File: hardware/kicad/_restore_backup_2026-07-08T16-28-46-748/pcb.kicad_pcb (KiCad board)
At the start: 2 copper layers, 56.1 x 59 mm, 7 parts, among them J1 ENCODER, J2 MOTOR, J3 12V MOTOR, U1 Dual_L298N_H_Bridge

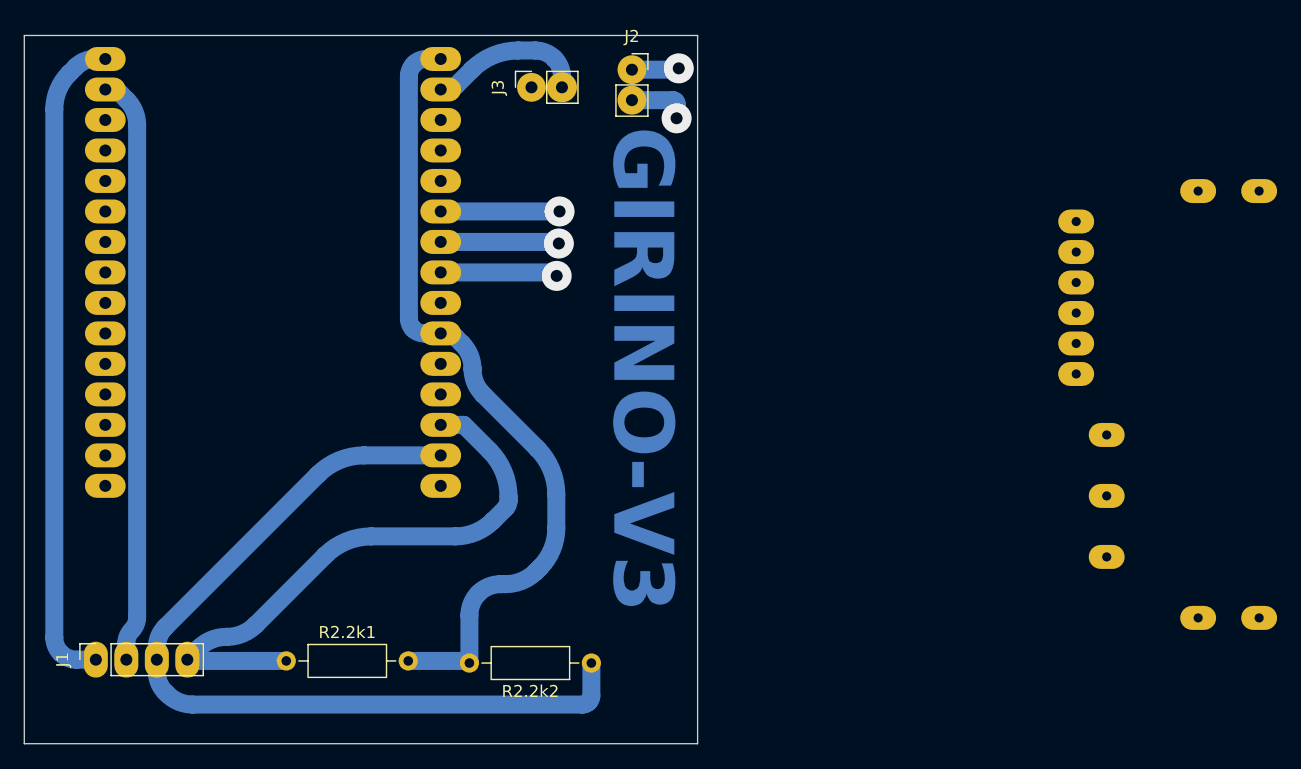
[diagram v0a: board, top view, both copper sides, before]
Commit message: fix:tirando o divisor de tensão e adcionando a forma correta de leitura do encoder
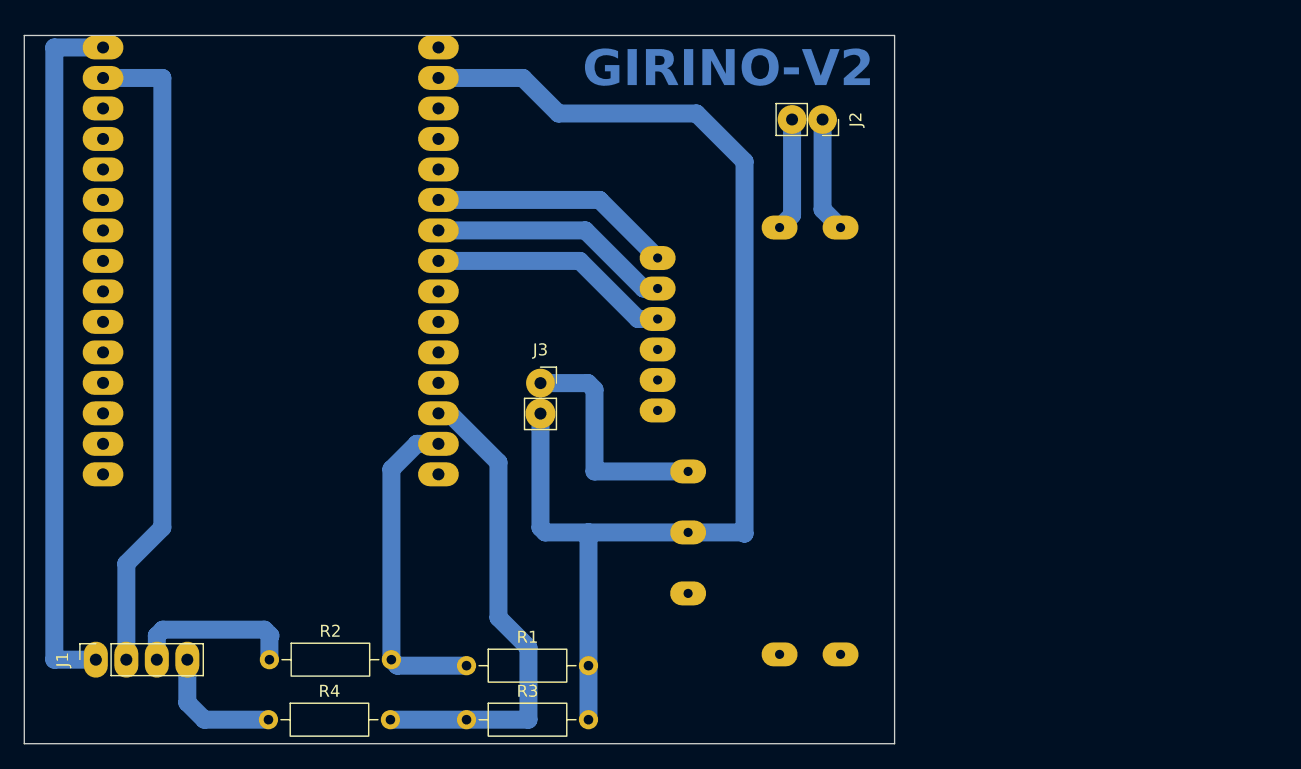
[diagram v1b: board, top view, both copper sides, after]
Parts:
- removed R2.2k1, R2.2k2: Resistor, Resistor_THT:R_Axial_DIN0207_L6.3mm_D2.5mm_P10.16mm_Horizontal
- added R1: 3,3k, Resistor_THT:R_Axial_DIN0207_L6.3mm_D2.5mm_P10.16mm_Horizontal, F.Cu at (96.8, 95.5)
- added R2: 2,2k, Resistor_THT:R_Axial_DIN0207_L6.3mm_D2.5mm_P10.16mm_Horizontal, F.Cu at (80.4, 95.0)
- added R3: 3,3k, Resistor_THT:R_Axial_DIN0207_L6.3mm_D2.5mm_P10.16mm_Horizontal, F.Cu at (96.8, 100.0)
- added R4: 2,2k, Resistor_THT:R_Axial_DIN0207_L6.3mm_D2.5mm_P10.16mm_Horizontal, F.Cu at (80.3, 100.0)
- moved U1 35.0 mm to (110.2, 97.1)
- moved J3 24.7 mm to (103.0, 72.0), turned to 0 degrees
- moved J2 16.4 mm to (126.5, 50.0), turned to -90 degrees
- moved A1 0.98 mm to (80.5, 61.8)
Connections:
- A1 pad 10: 3.3V -> unconnected-(A1-3V3-Pad10)
- J1 pad 3: Net-(A1-D1/GPIO5/SCL) -> Net-(J1-Pad3)
- J1 pad 4: Net-(A1-D2/GPIO4/SDA) -> Net-(J1-Pad4)
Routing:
- net GND: track 13.2 -> 101.7 mm
- net 3.3V: track 67.5 -> 0.00 mm
- net Net-(A1-D1/GPIO5/SCL): track 73.3 -> 27.1 mm
- net 12V: track 0.00 -> 19.3 mm
- net Net-(J1-Pad3): track 0.00 -> 13.9 mm
- net Net-(J1-Pad4): track 0.00 -> 10.9 mm
- net Net-(A1-D5/GPIO14/SCLK): track 9.76 -> 20.3 mm, vias 1 -> 0
- net Net-(A1-D6/GPIO12/MISO): track 9.88 -> 20.3 mm, vias 1 -> 0
- net Net-(A1-D7/GPIO13/MOSI/RX2): track 9.90 -> 20.3 mm, vias 1 -> 0
- net Net-(A1-D2/GPIO4/SDA): track 49.4 -> 40.7 mm
- net Net-(U1-OUTB2): track 3.94 -> 9.62 mm, vias 1 -> 0
- net Net-(A1-GND-Pad29): track 49.2 -> 54.6 mm
- net Net-(U1-OUTB1): track 5.09 -> 9.43 mm, vias 1 -> 0
- net VIN: track 55.2 -> 58.5 mm
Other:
- board size 56.1 x 59 mm -> 72.5 x 59 mm
- board text added: "GIRINO-V2"
- board text removed: "GIRINO-V3"
